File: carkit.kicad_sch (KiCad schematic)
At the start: 39 parts, among them J1 Barrel_Jack, J2 Conn_01x02_Pin, J3 Conn_02x03, J4 Conn_01x02_Pin, J5 Conn_01x02_Pin, P1 USB_C_Plug_USB2.0, SW1 SW_Push, SW2 SW_Push, U1 ESP32-C3-MINI-1, U2 LM2596SX-5.0/NOPB, U3 AMS1117-3.3, U4 DRV8876PWPR

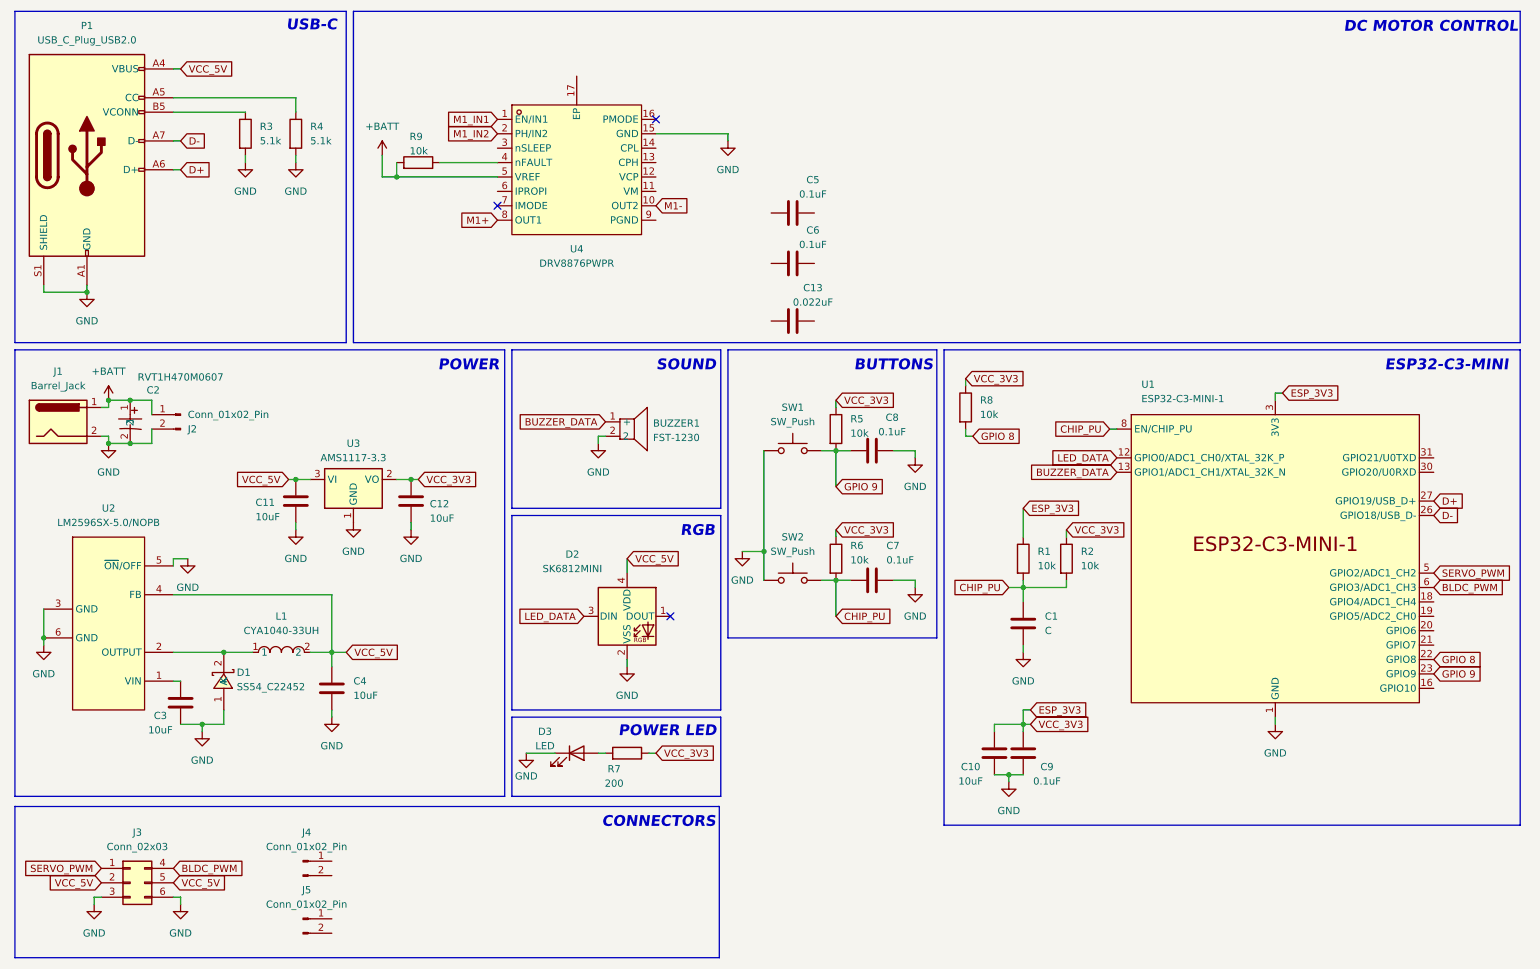
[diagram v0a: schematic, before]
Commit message: PCB routing completed
All components updated and the PCB should be fully functional.
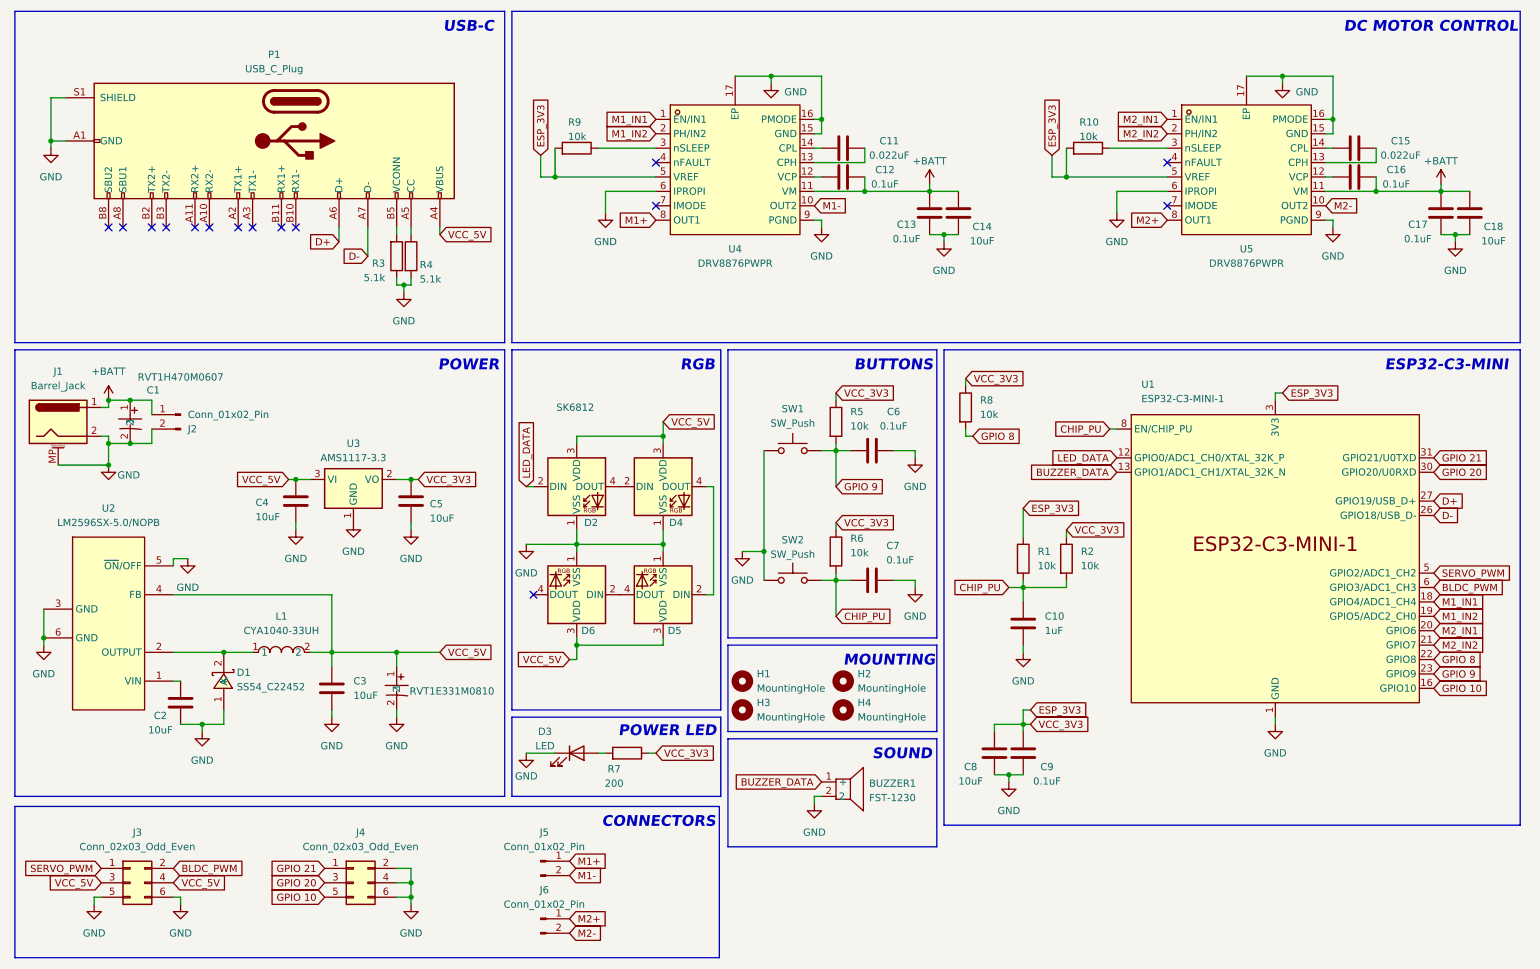
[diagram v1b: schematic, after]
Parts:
- removed D2: SK6812MINI, LED_SMD:LED_SK6812MINI_PLCC4_3.5x3.5mm_P1.75mm, symbol LED:SK6812MINI
- removed J1: Barrel_Jack, symbol Connector:Barrel_Jack
- removed J3: Conn_02x03, symbol Connector_Generic:Conn_02x03_Top_Bottom
- removed P1: USB_C_Plug_USB2.0, symbol Connector:USB_C_Plug_USB2.0
- added C12, C16, C17: 0.1uF, imported_components:C0805, symbol Device:C
- added C15: 0.022uF, imported_components:C0805, symbol Device:C
- added C18: 10uF, imported_components:C0805, symbol Device:C
- added C19: RVT1E331M0810, imported_components:CAP-SMD_BD8.0-L8.3-W8.3-LS9.3-FD-1, symbol imported_components:RVT1E331M0810_C335985
- added D2, D4, D5, D6: SK6812, LED_SMD:LED_SK6812_PLCC4_5.0x5.0mm_P3.2mm, symbol LED:SK6812
- added H1, H2, H3, H4: MountingHole, MountingHole:MountingHole_3.2mm_M3_Pad_Via, symbol Mechanical:MountingHole
- added J1: Barrel_Jack, imported_components:DC-IN-TH_DC-005-A200, symbol Connector:Barrel_Jack_MountingPin
- added J3, J4: Conn_02x03_Odd_Even, imported_components:HDR-SMD_6P-P2.54-V, symbol Connector_Generic:Conn_02x03_Odd_Even
- added P1: USB_C_Plug, imported_components:USB-C_SMD-TYPE-C-31-M-12, symbol Connector:USB_C_Plug
- added R10: 10k, imported_components:R0805, symbol Device:R
- added U5: DRV8876PWPR, imported_components:HTSSOP-16_L5.0-W4.4-P0.65-LS6.4-BL-EP, symbol imported_components:DRV8876PWPR
- C10: renamed from C1; value C -> 1uF; footprint (none) -> imported_components:C0805
- C11: renamed from C13; footprint (none) -> imported_components:C0805
- C13: renamed from C5; footprint (none) -> imported_components:C0805
- C14: renamed from C6; value 0.1uF -> 10uF; footprint (none) -> imported_components:C0805
- C2: renamed from C3; footprint (none) -> imported_components:C0805
- C3: renamed from C4; footprint (none) -> imported_components:C0805
- C4: renamed from C11; footprint (none) -> imported_components:C0805
- C5: renamed from C12; footprint (none) -> imported_components:C0805
- C6: renamed from C8; footprint (none) -> imported_components:C0805
- C7, C9: footprint (none) -> imported_components:C0805
- C8: renamed from C10; footprint (none) -> imported_components:C0805
- D3: footprint (none) -> imported_components:LED0805-RD
- J2: footprint (none) -> imported_components:CONN-TH_P5.00_KF301-5.0-2P
- J5: renamed from J4; footprint (none) -> imported_components:CONN-TH_P5.00_KF301-5.0-2P
- J6: renamed from J5; footprint (none) -> imported_components:CONN-TH_P5.00_KF301-5.0-2P
- R1, R2, R3, R4, R5, R6, R7, R8, R9: footprint (none) -> imported_components:R0805
- SW1, SW2: footprint (none) -> imported_components:SW-SMD_L3.9-W3.0-P4.45
- renumbered C2 to C1
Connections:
- net +BATT: now also C13.2, C14.2, U4.11 (VM), C12.1, C16.1, C17.2, C18.2, J1.1, U5.11 (VM); no longer R9.2, U4.5 (VREF)
- net BLDC_PWM: now also J3.2 (Pin_2)
- net CHIP_PU: now also SW2.1; no longer SW2.2
- net D+: now also P1.A6 (D+)
- net D-: now also P1.A7 (D-)
- net ESP_3V3: now also R9.2, U4.5 (VREF), R10.2, U5.5 (VREF)
- net GND: now also C13.1, C14.1, C6.2, R3.1, SW1.2, SW2.2, U4.16 (PMODE), U4.17 (EP), U4.6 (IPROPI), U4.9 (PGND), C17.1, C18.1, C19.2, D2.1 (VSS), D4.1 (VSS), D5.1 (VSS), D6.1 (VSS), J1.2, J1.MP (MountPin), J3.5 (Pin_5), J3.6 (Pin_6), J4.2 (Pin_2), J4.4 (Pin_4), J4.6 (Pin_6), P1.A1 (GND), P1.A12 (GND), P1.B1 (GND), P1.B12 (GND), P1.S1 (SHIELD), U5.15 (GND), U5.16 (PMODE), U5.17 (EP), U5.6 (IPROPI), U5.9 (PGND); no longer C6.1, R3.2, SW1.1, SW2.1
- net GPIO 9: now also C6.1, SW1.1; no longer C6.2, SW1.2
- net LED_DATA: now also D2.2 (DIN)
- net M1+: now also J5.1 (Pin_1)
- net M1-: now also J5.2 (Pin_2)
- net M1_IN1: now also U1.18 (GPIO4/ADC1_CH4)
- net M1_IN2: now also U1.19 (GPIO5/ADC2_CH0)
- net SERVO_PWM: now also J3.1 (Pin_1)
- net VCC_5V: now also C19.1, D2.3 (VDD), D4.3 (VDD), D5.3 (VDD), D6.3 (VDD), J3.3 (Pin_3), J3.4 (Pin_4), P1.A4 (VBUS), P1.A9 (VBUS), P1.B4 (VBUS), P1.B9 (VBUS)
- net at C11.1: now also U4.13 (CPH)
- net at C11.2: now also U4.14 (CPL)
- net at R4.1: now also P1.A5 (CC)
- net at R9.1: now also U4.3 (nSLEEP); no longer U4.4 (nFAULT)
- net at U4.12 (VCP): now also C12.2
- net M2+: now reaches J6.1 (Pin_1)
- net M2+: now also U5.8 (OUT1)
- net M2-: now reaches J6.2 (Pin_2)
- net M2-: now also U5.10 (OUT2)
- net GPIO 10: now reaches U1.16 (GPIO10)
- net GPIO 10: now also J4.5 (Pin_5)
- net M2_IN1: now reaches U1.20 (GPIO6)
- net M2_IN1: now also U5.1 (EN/IN1)
- net M2_IN2: now reaches U1.21 (GPIO7)
- net M2_IN2: now also U5.2 (PH/IN2)
- net GPIO 20: now reaches U1.30 (GPIO20/U0RXD)
- net GPIO 20: now also J4.3 (Pin_3)
- net GPIO 21: now reaches U1.31 (GPIO21/U0TXD)
- net GPIO 21: now also J4.1 (Pin_1)
- new net: R10.1, U5.3 (nSLEEP)
- new net: P1.B5 (VCONN), R3.2
- new net: D5.4 (DOUT), D6.2 (DIN)
- new net: C15.1, U5.13 (CPH)
- new net: C15.2, U5.14 (CPL)
- new net: D2.4 (DOUT), D4.2 (DIN)
- new net: D4.4 (DOUT), D5.2 (DIN)
- new net: C16.2, U5.12 (VCP)
- no-connect marks 3 -> 15
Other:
- note added: "MOUNTING"
- moved on the sheet: BUZZER1, C11, C13, C14, C6, J5, J6, R3, R4, R5, R6, R9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

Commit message: Panelization Complete
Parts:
- removed H4: MountingHole, MountingHole:MountingHole_3.2mm_M3_Pad_Via, symbol Mechanical:MountingHole
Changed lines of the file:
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@@
-	)
-	(symbol
-		(lib_id "Mechanical:MountingHole")
-		(at 162.56 139.7 0)
-		(unit 1)
-		(exclude_from_sim no)
-		(in_bom no)
-		(on_board yes)
-		(dnp no)
-		(fields_autoplaced yes)
-		(property "Reference" "H4"
-			(at 165.1 138.4299 0)
-			(effects
-				(font
-					(size 1.27 1.27)
-				)
-				(justify left)
-			)
-		)
-		(property "Value" "MountingHole"
-			(at 165.1 140.9699 0)
-			(effects
-				(font
-					(size 1.27 1.27)
-				)
-				(justify left)
-			)
-		)
-		(property "Footprint" "MountingHole:MountingHole_3.2mm_M3_Pad_Via"
-			(at 162.56 139.7 0)
-			(effects
-				(font
-					(size 1.27 1.27)
-				)
-				(hide yes)
-			)
-		)
-		(property "Datasheet" "~"
-			(at 162.56 139.7 0)
-			(effects
-				(font
-					(size 1.27 1.27)
-				)
-				(hide yes)
-			)
-		)
-		(property "Description" "Mounting Hole without connection"
-			(at 162.56 139.7 0)
-			(effects
-				(font
-					(size 1.27 1.27)
-				)
-				(hide yes)
-			)
-		)
-		(instances
-			(project "carkit"
-				(path "/44619ab4-8ea1-4cc9-b8b1-3e8f0ceb2a27"
-					(reference "H4")
-					(unit 1)
-				)
-			)
-		)
 	)
 	(symbol

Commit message: Quick fix
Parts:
- added SW3: SW_SPDT, imported_components:SW-SMD_MST-12D18G4-SPDT-SLIDE-SWITCH, symbol Switch:SW_SPDT
- J2: value Conn_01x02_Pin -> Conn_01x02
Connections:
- net +BATT: now also SW3.3 (C); no longer C1.1, C12.1, C13.2, C14.2, C16.1, C17.2, C18.2, U4.11 (VM), U5.11 (VM)
- net REG_BATT+: now reaches C2.2, U2.1 (VIN)
- net REG_BATT+: now also C1.1, C12.1, C13.2, C14.2, C16.1, C17.2, C18.2, U4.11 (VM), U5.11 (VM), SW3.2 (B)
- no-connect marks 15 -> 16
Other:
- moved on the sheet: C1, C4, C5, J2, U3
